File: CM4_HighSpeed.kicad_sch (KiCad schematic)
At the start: 13 parts, among them J10 690-019-298-412, J15 Conn_01x22_Female, J16 Conn_01x22_Female, J22 690-019-298-412, J4 Conn_01x22_Female, J5 Conn_01x22_Female, J6 THD-02-R, U12 RT9742SNGV

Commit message: removed both HDMI ports and connections from CM4 Highspeed schematic and pcb
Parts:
- removed C13: 100n, Capacitor_SMD:C_0402_1005Metric, symbol Device:C
- removed J10, J22: 690-019-298-412, CM4IO:EDAC 690-019-298-412, symbol CM4IO:HDMI_A_1.4
- C12: value 100n -> (none); footprint Capacitor_SMD:C_0402_1005Metric -> (none)
- J15, J16, J4, J5: value Conn_01x22_Female -> (none); footprint Connector_FFC-FPC:Hirose_FH12-22S-0.5SH_1x22-1MP_P0.50mm_Horizontal -> (none)
- J6: value THD-02-R -> (none); footprint Connector_PinHeader_2.54mm:PinHeader_2x02_P2.54mm_Vertical -> (none)
- Module1: value ComputeModule4 -> (none); footprint CM4IO:Raspberry-Pi-4-Compute-Module -> (none)
- R6, R7: value 2.2K 1% -> (none); footprint Resistor_SMD:R_0402_1005Metric -> (none)
- U12: value RT9742SNGV -> (none); footprint Package_TO_SOT_SMD:SOT-23 -> (none)
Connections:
- net HDMI0_CEC: no longer names the net of Module1.151 (HDMI0_CEC)
- net HDMI0_CK_N: no longer names the net of Module1.190 (HDMI0_CLK_N)
- net HDMI0_CK_P: no longer names the net of Module1.188 (HDMI0_CLK_P)
- net HDMI0_D0_N: no longer names the net of Module1.184 (HDMI0_TX0_N)
- net HDMI0_D0_P: no longer names the net of Module1.182 (HDMI0_TX0_P)
- net HDMI0_D1_N: no longer names the net of Module1.178 (HDMI0_TX1_N)
- net HDMI0_D1_P: no longer names the net of Module1.176 (HDMI0_TX1_P)
- net HDMI0_D2_N: no longer names the net of Module1.172 (HDMI0_TX2_N)
- net HDMI0_D2_P: no longer names the net of Module1.170 (HDMI0_TX2_P)
- net HDMI0_HOTPLUG: no longer names the net of Module1.153 (HDMI0_HOTPLUG)
- net HDMI0_SCL: no longer names the net of Module1.200 (HDMI0_SCL)
- net HDMI0_SDA: no longer names the net of Module1.199 (HDMI0_SDA)
- net HDMI1_CEC: no longer names the net of Module1.149 (HDMI1_CEC)
- net HDMI1_CK_N: no longer names the net of Module1.166 (HDMI1_CLK_N)
- net HDMI1_CK_P: no longer names the net of Module1.164 (HDMI1_CLK_P)
- net HDMI1_D0_N: no longer names the net of Module1.160 (HDMI1_TX0_N)
- net HDMI1_D0_P: no longer names the net of Module1.158 (HDMI1_TX0_P)
- net HDMI1_D1_N: no longer names the net of Module1.154 (HDMI1_TX1_N)
- net HDMI1_D1_P: no longer names the net of Module1.152 (HDMI1_TX1_P)
- net HDMI1_D2_N: no longer names the net of Module1.148 (HDMI1_TX2_N)
- net HDMI1_D2_P: no longer names the net of Module1.146 (HDMI1_TX2_P)
- net HDMI1_HOTPLUG: no longer names the net of Module1.143 (HDMI1_HOTPLUG)
- net HDMI1_SCL: no longer names the net of Module1.147 (HDMI1_SCL)
- net HDMI1_SDA: no longer names the net of Module1.145 (HDMI1_SDA)
- net HDMI_5v: no longer names the net of U12.2 (OUT)
- no-connect marks 18 -> 16

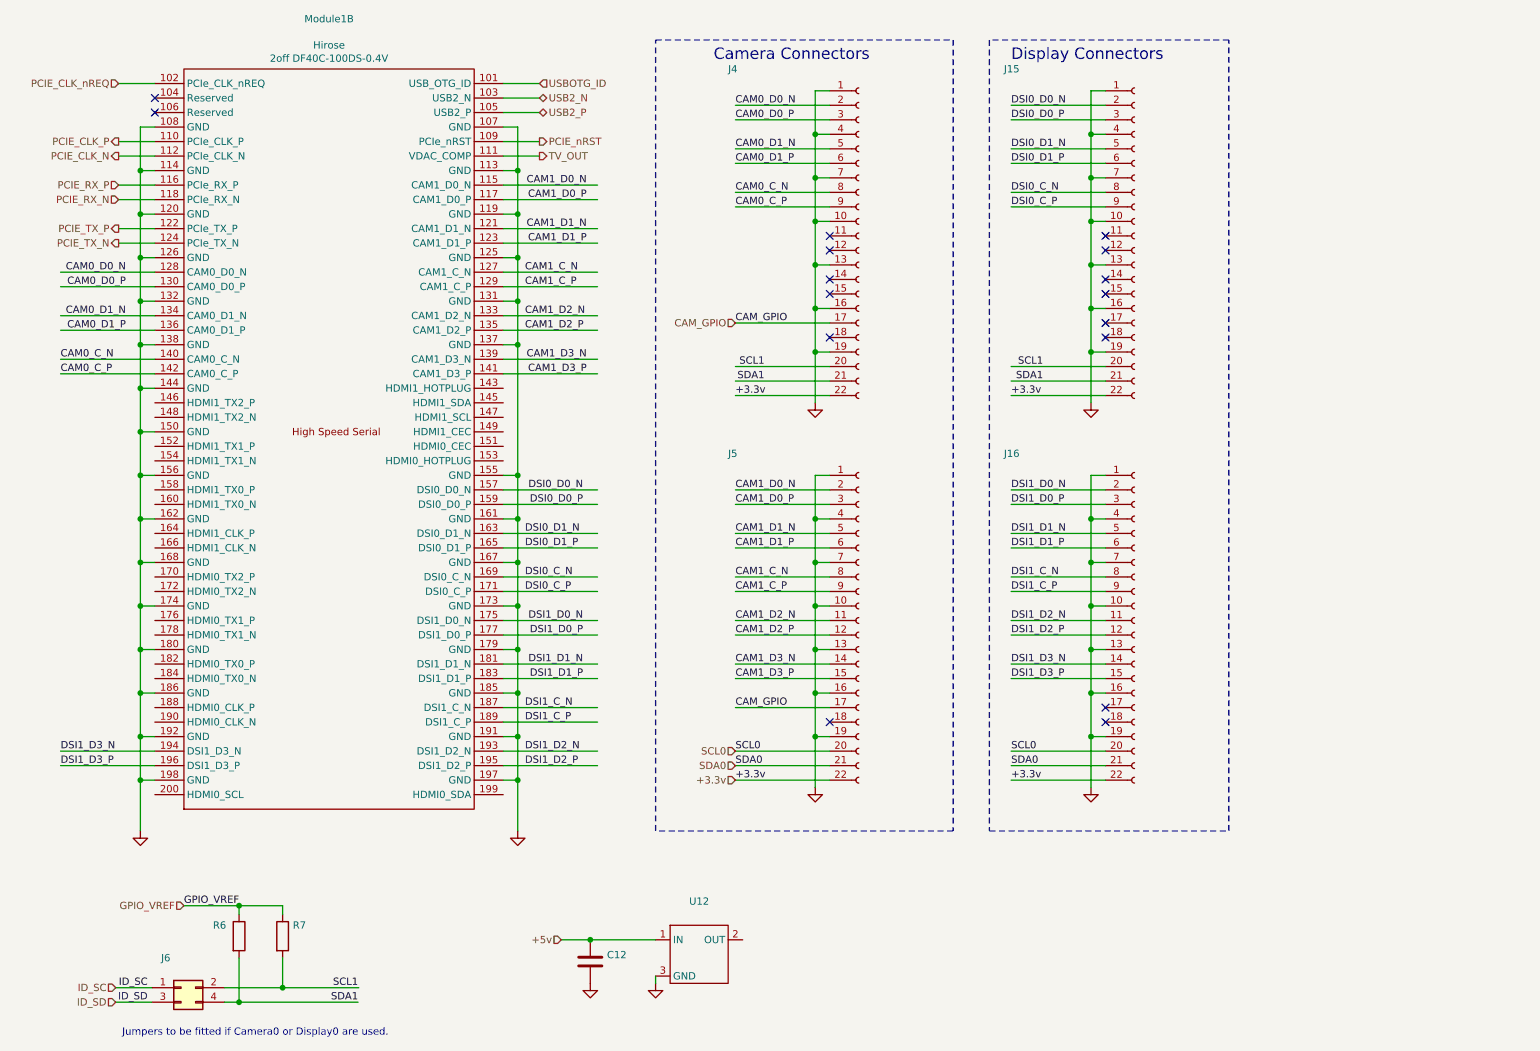
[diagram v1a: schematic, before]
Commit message: removed camera connector, ethernet ports and connections from CM4 Highspeed schematic and pcb. Re-arranged some traces and vias
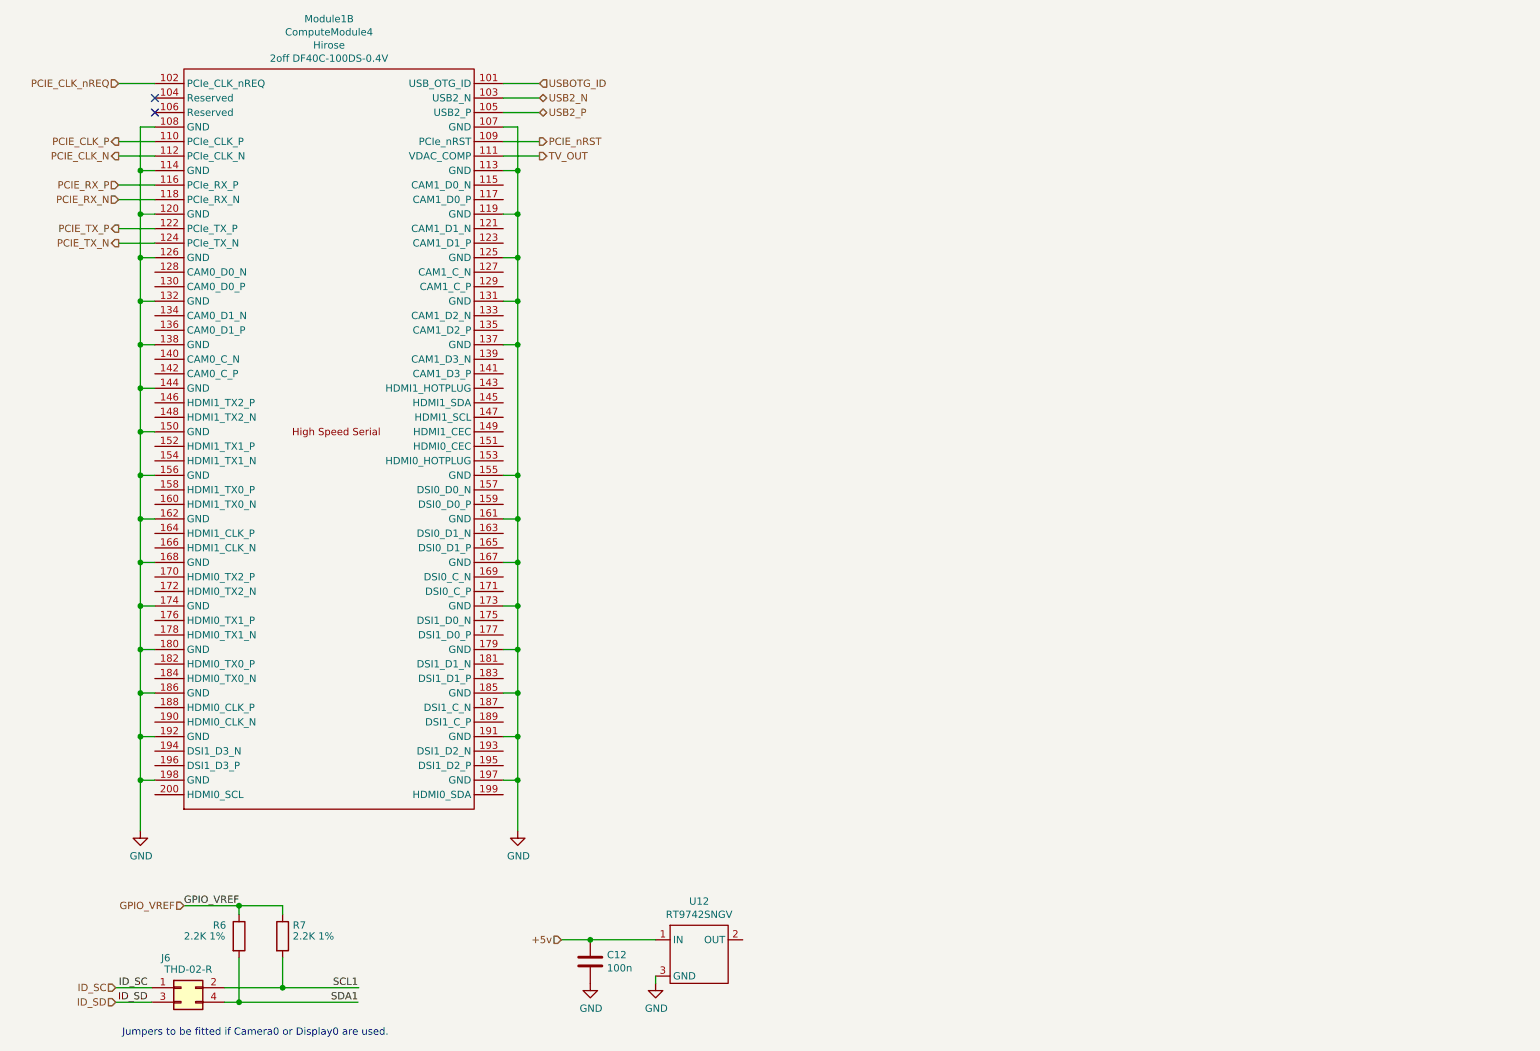
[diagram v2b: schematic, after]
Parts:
- removed J15, J16, J4, J5: (no value), symbol Connector:Conn_01x22_Female
- C12: value (none) -> 100n; footprint (none) -> Capacitor_SMD:C_0402_1005Metric
- J6: value (none) -> THD-02-R; footprint (none) -> Connector_PinHeader_2.54mm:PinHeader_2x02_P2.54mm_Vertical
- Module1: value (none) -> ComputeModule4; footprint (none) -> CM4IO:Raspberry-Pi-4-Compute-Module
- R6, R7: value (none) -> 2.2K 1%; footprint (none) -> Resistor_SMD:R_0402_1005Metric
- U12: value (none) -> RT9742SNGV; footprint (none) -> Package_TO_SOT_SMD:SOT-23
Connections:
- net CAM0_C_N: no longer names the net of Module1.140 (CAM0_C_N)
- net CAM0_C_P: no longer names the net of Module1.142 (CAM0_C_P)
- net CAM0_D0_N: no longer names the net of Module1.128 (CAM0_D0_N)
- net CAM0_D0_P: no longer names the net of Module1.130 (CAM0_D0_P)
- net CAM0_D1_N: no longer names the net of Module1.134 (CAM0_D1_N)
- net CAM0_D1_P: no longer names the net of Module1.136 (CAM0_D1_P)
- net CAM1_C_N: no longer names the net of Module1.127 (CAM1_C_N)
- net CAM1_C_P: no longer names the net of Module1.129 (CAM1_C_P)
- net CAM1_D0_N: no longer names the net of Module1.115 (CAM1_D0_N)
- net CAM1_D0_P: no longer names the net of Module1.117 (CAM1_D0_P)
- net CAM1_D1_N: no longer names the net of Module1.121 (CAM1_D1_N)
- net CAM1_D1_P: no longer names the net of Module1.123 (CAM1_D1_P)
- net CAM1_D2_N: no longer names the net of Module1.133 (CAM1_D2_N)
- net CAM1_D2_P: no longer names the net of Module1.135 (CAM1_D2_P)
- net CAM1_D3_N: no longer names the net of Module1.139 (CAM1_D3_N)
- net CAM1_D3_P: no longer names the net of Module1.141 (CAM1_D3_P)
- net DSI0_C_N: no longer names the net of Module1.169 (DSI0_C_N)
- net DSI0_C_P: no longer names the net of Module1.171 (DSI0_C_P)
- net DSI0_D0_N: no longer names the net of Module1.157 (DSI0_D0_N)
- net DSI0_D0_P: no longer names the net of Module1.159 (DSI0_D0_P)
- net DSI0_D1_N: no longer names the net of Module1.163 (DSI0_D1_N)
- net DSI0_D1_P: no longer names the net of Module1.165 (DSI0_D1_P)
- net DSI1_C_N: no longer names the net of Module1.187 (DSI1_C_N)
- net DSI1_C_P: no longer names the net of Module1.189 (DSI1_C_P)
- net DSI1_D0_N: no longer names the net of Module1.175 (DSI1_D0_N)
- net DSI1_D0_P: no longer names the net of Module1.177 (DSI1_D0_P)
- net DSI1_D1_N: no longer names the net of Module1.181 (DSI1_D1_N)
- net DSI1_D1_P: no longer names the net of Module1.183 (DSI1_D1_P)
- net DSI1_D2_N: no longer names the net of Module1.193 (DSI1_D2_N)
- net DSI1_D2_P: no longer names the net of Module1.195 (DSI1_D2_P)
- net DSI1_D3_N: no longer names the net of Module1.194 (DSI1_D3_N)
- net DSI1_D3_P: no longer names the net of Module1.196 (DSI1_D3_P)
- no-connect marks 16 -> 2
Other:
- note removed: "Camera Connectors"
- note removed: "Display Connectors"
